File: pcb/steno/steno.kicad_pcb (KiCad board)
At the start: 2 copper layers, 200 x 50 mm, 59 parts, among them J1 Conn_01x02, K1 KEYSW, K10 KEYSW, K11 KEYSW, K12 KEYSW, K13 KEYSW, K14 KEYSW, K15 KEYSW, K16 KEYSW, K17 KEYSW, K18 KEYSW, K19 KEYSW, K2 KEYSW, K20 KEYSW, K21 KEYSW, K22 KEYSW, K23 KEYSW, K24 KEYSW, K25 KEYSW, K26 KEYSW, K27 KEYSW, K28 KEYSW, K3 KEYSW, K4 KEYSW, K5 KEYSW, K6 KEYSW, K7 KEYSW, K8 KEYSW, K9 KEYSW, U1 Adafruit_Feather

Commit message: Remove v1 files
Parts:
- removed the K2 at (70.0, 84.3)
- removed REF**: D_DO-34_SOD68_P7.62mm_Horizontal, Diode_THT:D_DO-34_SOD68_P7.62mm_Horizontal
- added D29: DIODE, Diode_THT:D_DO-34_SOD68_P7.62mm_Horizontal, B.Cu at (184.5, 95.2)
- added D30: DIODE, Diode_THT:D_DO-34_SOD68_P7.62mm_Horizontal, B.Cu at (180.7, 96.5)
- added J2: Conn_01x04, steno:OLED, F.Cu at (176.7, 112.6)
- added K1: KEYSW, Keebio-Parts:Kailh-PG1350-1u-No-Clickhole, F.Cu at (48.9, 56.9)
- added K29: KEYSW, Keebio-Parts:Kailh-PG1350-1u-No-Clickhole, F.Cu at (197.9, 78.6)
- added K30: KEYSW, Keebio-Parts:Kailh-PG1350-1u-No-Clickhole, F.Cu at (180.8, 84.3)
- added U2: MT25QL128ABA1ESE, Package_SO:SOP-8_5.28x5.23mm_P1.27mm, F.Cu at (158.2, 125.1)
- D1, D10, D11, D12, D13, D14, D15, D16, D17, D18, D19, D2, D20, D21, D22, D23, D24, D25, D26, D27, D28, D3, D4, D5, D6, D7, D8, D9: footprint Diode_SMD:D_SOD-123F -> Diode_THT:D_DO-34_SOD68_P7.62mm_Horizontal
- J1: footprint Connector_JST:JST_PH_B2B-PH-SM4-TB_1x02-1MP_P2.00mm_Vertical -> Connector_PinHeader_2.54mm:PinHeader_1x02_P2.54mm_Vertical; moved to F.Cu
- moved K25 153.5 mm to (271.9, 73.0), turned to 198.4 degrees
- moved K8 120.6 mm to (60.6, 78.7), turned to 161.6 degrees
- moved K7 119.6 mm to (43.5, 73.0), turned to 161.6 degrees
- moved K11 119.1 mm to (117.5, 78.6), turned to 161.6 degrees
- moved K23 118.5 mm to (192.5, 62.5), turned to 198.4 degrees
- moved K26 118.0 mm to (254.8, 78.7), turned to 198.4 degrees
- moved K9 117.4 mm to (83.4, 67.3), turned to 161.6 degrees
- moved K10 116.9 mm to (102.3, 67.3), turned to 161.6 degrees
- moved D11 107.8 mm to (132.9, 95.9), turned to 251.6 degrees
- moved K19 96.6 mm to (266.5, 56.8), turned to 198.4 degrees
- moved D23 94.0 mm to (182.6, 95.9), turned to 288.4 degrees
- moved D10 94.0 mm to (129.1, 94.6), turned to 251.6 degrees
- moved K16 89.3 mm to (214.5, 109.5), turned to 198.4 degrees
- moved K27 86.8 mm to (232.1, 67.3), turned to 198.4 degrees
- moved K24 85.4 mm to (175.5, 68.2), turned to 198.4 degrees
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- renumbered K1 to K2
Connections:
- D10 pad 2: COL10 -> COL4
- D11 pad 2: COL11 -> COL5
- D12 pad 2: COL1 -> COL6
- D13 pad 2: COL2 -> COL1
- D14 pad 2: COL3 -> COL2
- D15 pad 2: COL4 -> COL3
- D16 pad 2: COL5 -> COL4
- D17 pad 2: COL6 -> COL5
- D18 pad 2: COL7 -> COL6
- D19 pad 2: COL8 -> COL1
- D20 pad 2: COL9 -> COL2
- D21 pad 2: COL10 -> COL3
- D22 pad 2: COL11 -> COL4
- D23 pad 2: COL3 -> COL5
- D24 pad 2: COL4 -> COL6
- D25 pad 2: COL5 -> COL1
- D26 pad 2: COL6 -> COL2
- D27 pad 2: COL7 -> COL3
- D28 pad 2: COL8 -> COL4
- D7 pad 2: COL7 -> COL1
- D8 pad 2: COL8 -> COL2
- D9 pad 2: COL9 -> COL3
- J1 pad 1: GND -> BAT
- J1 pad 2: BAT -> GND
- K10 pad 1: ROW1 -> ROW2
- K11 pad 1: ROW1 -> ROW2
- K13 pad 1: ROW2 -> ROW3
- K14 pad 1: ROW2 -> ROW3
- K15 pad 1: ROW2 -> ROW3
- K16 pad 1: ROW2 -> ROW3
- K17 pad 1: ROW2 -> ROW3
- K18 pad 1: ROW2 -> ROW3
- K19 pad 1: ROW2 -> ROW4
- K2 pad 2: Net-(D1-Pad1) -> Net-(D2-Pad1)
- K20 pad 1: ROW2 -> ROW4
- K21 pad 1: ROW2 -> ROW4
- K22 pad 1: ROW2 -> ROW4
- K23 pad 1: ROW3 -> ROW4
- K24 pad 1: ROW3 -> ROW4
- K25 pad 1: ROW3 -> ROW5
- K26 pad 1: ROW3 -> ROW5
- K27 pad 1: ROW3 -> ROW5
- K28 pad 1: ROW3 -> ROW5
- K7 pad 1: ROW1 -> ROW2
- K8 pad 1: ROW1 -> ROW2
- K9 pad 1: ROW1 -> ROW2
- U1 pad 1: Net-(U1-Pad1) -> (no net)
- U1 pad 10: ROW3 -> COL3
- U1 pad 11: ROW2 -> COL2
- U1 pad 12: ROW1 -> COL1
- U1 pad 14: Net-(U1-Pad14) -> (no net)
- U1 pad 15: Net-(U1-Pad15) -> VCC
- U1 pad 16: RST -> (no net)
- U1 pad 18: GND -> (no net)
- U1 pad 19: Net-(U1-Pad19) -> (no net)
- U1 pad 2: COL5 -> DQ3
- U1 pad 20: Net-(U1-Pad20) -> ROW1
- U1 pad 21: Net-(U1-Pad21) -> ROW2
- U1 pad 22: COL11 -> ROW4
- U1 pad 23: COL10 -> ROW5
- U1 pad 24: Net-(U1-Pad24) -> (no net)
- U1 pad 25: COL9 -> ROW3
- U1 pad 26: COL8 -> CS
- U1 pad 27: COL7 -> SCL
- U1 pad 28: COL6 -> SDA
- U1 pad 3: COL4 -> DQ2
- U1 pad 4: Net-(U1-Pad4) -> MISO_DQ1
- U1 pad 5: Net-(U1-Pad5) -> MOSI_DQ0
- U1 pad 6: Net-(U1-Pad6) -> SCLK
- U1 pad 7: COL3 -> COL6
- U1 pad 8: COL2 -> COL5
- U1 pad 9: COL1 -> COL4
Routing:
- net ROW4: track 0.00 -> 156.3 mm, vias 0 -> 1
- net ROW5: track 0.00 -> 144.9 mm, vias 0 -> 1
- net COL11: track 88.5 -> 0.00 mm, vias 1 -> 0
- net VCC: track 0.00 -> 76.4 mm
- net Net-(D25-Pad1): track 10.9 -> 84.8 mm
- net Net-(D19-Pad1): track 17.5 -> 89.2 mm
- net COL10: track 69.5 -> 0.00 mm, vias 1 -> 0
- net COL5: track 10.1 -> 65.9 mm
- net Net-(D20-Pad1): track 17.2 -> 70.3 mm
- net COL9: track 50.5 -> 0.00 mm, vias 1 -> 0
- net Net-(D26-Pad1): track 14.5 -> 64.2 mm
- net Net-(D1-Pad1): track 33.0 -> 82.4 mm
- net Net-(D21-Pad1): track 17.5 -> 63.7 mm
- net COL4: track 27.8 -> 72.6 mm, vias 1 -> 0
- net COL6: track 10.8 -> 55.6 mm
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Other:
- board size 200 x 50 mm -> 250.8 x 91.5 mm
- board text added: "BAT"
- board text added: "GND"

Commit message: Update PCB
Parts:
- D1, D10, D11, D12, D13, D14, D15, D16, D17, D18, D19, D2, D20, D21, D22, D23, D24, D25, D26, D27, D28, D29, D3, D30, D4, D5, D6, D7, D8, D9: footprint Diode_THT:D_DO-34_SOD68_P7.62mm_Horizontal -> Diode_SMD:D_SOD-123; moved to F.Cu
- U1: value Adafruit_Feather -> nice_nano; footprint Downloads:ADAFRUIT_FEATHER -> nice-nano-kicad:nice_nano
- moved D19 74.5 mm to (249.0, 32.1), turned to 216.8 degrees
- moved D7 71.1 mm to (46.5, 116.5), turned to 180 degrees
- moved D25 70.6 mm to (259.2, 45.7), turned to 216.8 degrees
- moved D1 68.2 mm to (46.5, 99.5), turned to 180 degrees
- moved D8 60.6 mm to (64.5, 116.5), turned to 180 degrees
- moved D20 60.5 mm to (234.6, 42.9), turned to 216.8 degrees
- moved D2 57.5 mm to (64.5, 99.5), turned to 180 degrees
- moved D26 56.3 mm to (244.8, 56.5), turned to 216.8 degrees
- moved D21 55.1 mm to (209.4, 39.2), turned to 216.8 degrees
- moved D22 48.9 mm to (191.4, 45.2), turned to 216.8 degrees
- moved D27 45.3 mm to (219.6, 52.8), turned to 216.8 degrees
- moved D3 44.4 mm to (82.5, 81.5), turned to 180 degrees
- moved D15 44.4 mm to (148.5, 133.0), turned to 180 degrees
- moved D14 44.0 mm to (130.5, 133.0), turned to 180 degrees
- moved D13 42.9 mm to (112.5, 133.0), turned to 180 degrees
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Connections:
- U1 pad 1: (no net) -> ROW1
- U1 pad 10: COL3 -> COL6
- U1 pad 11: COL2 -> Net-(U1-Pad11)
- U1 pad 12: COL1 -> CS
- U1 pad 13: GND -> ROW3
- U1 pad 14: (no net) -> MOSI_DQ0
- U1 pad 15: VCC -> MISO_DQ1
- U1 pad 16: (no net) -> SCLK
- U1 pad 17: BAT -> COL2
- U1 pad 18: (no net) -> COL1
- U1 pad 19: (no net) -> ROW4
- U1 pad 2: DQ3 -> ROW2
- U1 pad 20: ROW1 -> ROW5
- U1 pad 21: ROW2 -> VCC
- U1 pad 22: ROW4 -> RST
- U1 pad 23: ROW5 -> GND
- U1 pad 24: (no net) -> BAT
- U1 pad 3: DQ2 -> GND
- U1 pad 4: MISO_DQ1 -> GND
- U1 pad 5: MOSI_DQ0 -> SCL
- U1 pad 6: SCLK -> SDA
- U1 pad 7: COL6 -> COL3
- U1 pad 8: COL5 -> COL4
- U1 pad 9: COL4 -> COL5
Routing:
- net COL1: track 102.0 -> 297.2 mm, vias 0 -> 2
- net COL2: track 90.2 -> 263.9 mm, vias 0 -> 2
- net COL3: track 80.5 -> 248.4 mm, vias 0 -> 2
- net COL4: track 72.6 -> 214.5 mm, vias 0 -> 2
- net COL5: track 65.9 -> 173.4 mm, vias 0 -> 2
- net COL6: track 55.6 -> 144.5 mm, vias 0 -> 2
- net Net-(D19-Pad1): track 89.2 -> 9.69 mm
- net Net-(D25-Pad1): track 84.8 -> 9.69 mm
- net Net-(D1-Pad1): track 82.4 -> 9.69 mm
- net Net-(D7-Pad1): track 71.3 -> 9.69 mm
- net Net-(D20-Pad1): track 70.3 -> 9.69 mm
- net Net-(D3-Pad1): track 65.3 -> 9.69 mm
- net Net-(D26-Pad1): track 64.2 -> 9.69 mm
- net Net-(D21-Pad1): track 63.7 -> 9.69 mm
- net Net-(D2-Pad1): track 62.9 -> 9.69 mm
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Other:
- board size 250.8 x 91.5 mm -> 231.4 x 120.7 mm

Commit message: First PCB version
- Use raw MCU
- Use 5x6 matrix and 30keys (like steno phone)
- Use SOD-123 diodes (like steno phone)
- Use 2.2in TFT for better UX(?)
- Lots of ground plane!
- Add (fake?) logo and contributors
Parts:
- removed J2: Conn_01x04, steno:OLED
- added C1: 22pF, Capacitor_SMD:C_0603_1608Metric, F.Cu at (133.5, 110.0)
- added C10: 1uF, Capacitor_SMD:C_0805_2012Metric, F.Cu at (159.0, 115.5)
- added C11: 1uF, Capacitor_SMD:C_0805_2012Metric, F.Cu at (158.0, 120.5)
- added C2: 22pF, Capacitor_SMD:C_0603_1608Metric, F.Cu at (133.5, 100.0)
- added C3: 1uF, Capacitor_SMD:C_0805_2012Metric, F.Cu at (156.0, 102.0)
- added C4: 1uF, Capacitor_SMD:C_0805_2012Metric, F.Cu at (146.5, 96.0)
- added C5: 0.1uF, Capacitor_SMD:C_0603_1608Metric, F.Cu at (138.5, 103.0)
- added C6: 0.1uF, Capacitor_SMD:C_0603_1608Metric, F.Cu at (155.0, 98.0)
- added C7: 0.1uF, Capacitor_SMD:C_0603_1608Metric, F.Cu at (143.0, 114.0)
- added C8: 10uF, Capacitor_SMD:C_0805_2012Metric, F.Cu at (156.0, 109.0)
- added C9: 1uF, Capacitor_SMD:C_0805_2012Metric, F.Cu at (160.0, 108.0)
- added F1: Polyfuse_Small, Fuse:Fuse_1206_3216Metric_Castellated, F.Cu at (151.0, 76.5)
- added G***: LOGO, misc:batwings, F.Cu at (196.0, 98.5)
- added R1: 10k, Resistor_SMD:R_0805_2012Metric, F.Cu at (144.0, 78.0)
- added R2: 22, Resistor_SMD:R_0603_1608Metric, F.Cu at (148.2, 84.9)
- added R3: 22, Resistor_SMD:R_0603_1608Metric, F.Cu at (149.7, 84.9)
- added R4: 10k, Resistor_SMD:R_0805_2012Metric, F.Cu at (156.0, 112.0)
- added R5: 10k, Resistor_SMD:R_0805_2012Metric, F.Cu at (153.4, 128.0)
- added SW1: SW_Push, Button_Switch_SMD:SW_SPST_B3U-1000P, F.Cu at (140.5, 69.7)
- added U3: MCP1700-3302E_SOT23, Package_TO_SOT_SMD:SOT-23, F.Cu at (160.0, 111.0)
- added U4: LCD2.2in, steno:LCD2.2in, F.Cu at (148.5, 105.1)
- added Y1: 16MHz, Crystal:Crystal_SMD_EuroQuartz_MJ-4Pin_5.0x3.2mm_HandSoldering, F.Cu at (133.5, 105.0)
- J1: value Conn_01x02 -> USB_mini_micro_B; footprint Connector_PinHeader_2.54mm:PinHeader_1x02_P2.54mm_Vertical -> Connector_USB:AMPHENOL_10118192-0001LF
- K1, K10, K11, K12, K13, K14, K15, K16, K17, K18, K19, K2, K20, K21, K22, K23, K24, K25, K26, K27, K28, K29, K3, K30, K4, K5, K6, K7, K8, K9: value KEYSW -> SW_Push
- U1: value nice_nano -> ATmega32U4-AU; footprint nice-nano-kicad:nice_nano -> Package_QFP:TQFP-44_10x10mm_P0.8mm
- moved D7 43.2 mm to (21.6, 81.1), turned to 161.6 degrees
- moved K7 42.2 mm to (23.0, 76.9), turned to 161.6 degrees
- moved D1 39.6 mm to (26.9, 65.0), turned to 161.6 degrees
- moved K19 39.3 mm to (268.8, 60.7), turned to 198.4 degrees
- moved D8 39.3 mm to (38.7, 86.8), turned to 161.6 degrees
- moved D19 39.1 mm to (270.2, 65.0), turned to 198.4 degrees
- moved D25 39.0 mm to (275.6, 81.1), turned to 198.4 degrees
- moved K25 39.0 mm to (274.1, 76.9), turned to 198.4 degrees
- moved K1 38.7 mm to (28.4, 60.7), turned to 161.6 degrees
- moved K8 38.2 mm to (40.1, 82.5), turned to 161.6 degrees
- moved D13 35.3 mm to (80.4, 118.1), turned to 161.6 degrees
- moved D2 35.3 mm to (44.0, 70.7), turned to 161.6 degrees
- moved K2 34.3 mm to (45.4, 66.4), turned to 161.6 degrees
- moved D14 34.2 mm to (97.5, 123.8), turned to 161.6 degrees
- moved D15 34.1 mm to (114.6, 129.5), turned to 161.6 degrees
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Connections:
- net RST renamed Net-(U1-Pad22)
- J1 pad 1: BAT -> VCC
- J1 pad 2: GND -> D-
- U1 pad 1: ROW1 -> Net-(U1-Pad1)
- U1 pad 10: COL6 -> MOSI
- U1 pad 11: Net-(U1-Pad11) -> MISO
- U1 pad 12: CS -> Net-(U1-Pad12)
- U1 pad 13: ROW3 -> Net-(R1-Pad1)
- U1 pad 14: MOSI_DQ0 -> +5V
- U1 pad 15: MISO_DQ1 -> GND
- U1 pad 16: SCLK -> Net-(C2-Pad1)
- U1 pad 17: COL2 -> Net-(C1-Pad1)
- U1 pad 18: COL1 -> LITE
- U1 pad 19: ROW4 -> ROW1
- U1 pad 2: ROW2 -> +5V
- U1 pad 20: ROW5 -> ROW2
- U1 pad 21: VCC -> ROW3
- U1 pad 24: BAT -> +5V
- U1 pad 3: GND -> Net-(R3-Pad1)
- U1 pad 30: GND -> COL6
- U1 pad 31: Net-(U1-Pad31) -> CS
- U1 pad 32: DQ3 -> Net-(U1-Pad32)
- U1 pad 33: DQ2 -> Net-(R4-Pad2)
- U1 pad 34: BAT -> +5V
- U1 pad 4: GND -> Net-(R2-Pad1)
- U1 pad 5: SCL -> GND
- U1 pad 6: SDA -> Net-(C4-Pad1)
- U1 pad 7: COL3 -> +5V
- U1 pad 8: COL4 -> Net-(U1-Pad8)
- U1 pad 9: COL5 -> SCLK
- U2 pad 2: MISO_DQ1 -> MISO
- U2 pad 3: DQ2 -> Net-(R5-Pad1)
- U2 pad 4: GND -> GND1
- U2 pad 5: MOSI_DQ0 -> MOSI
- U2 pad 7: DQ3 -> Net-(R5-Pad1)
- U2 pad 8: VCC -> +3V3
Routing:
- net +5V: track 0.00 -> 98.9 mm, vias 0 -> 8
- net VCC: track 50.2 -> 4.31 mm
- net MISO: track 0.00 -> 45.8 mm, vias 0 -> 3
- net LCD_CS: track 0.00 -> 45.0 mm, vias 0 -> 1
- net MOSI: track 0.00 -> 44.8 mm, vias 0 -> 2
- net C\D: track 0.00 -> 44.4 mm, vias 0 -> 1
- net LCD_RST: track 0.00 -> 44.0 mm, vias 0 -> 1
- net Net-(R1-Pad1): track 0.00 -> 38.6 mm
- net SDA: track 37.5 -> 0.00 mm
- net SCL: track 37.1 -> 0.00 mm
- net GND: track 74.0 -> 108.0 mm, vias 0 -> 11
- net COL1: track 297.2 -> 330.5 mm, vias 2 -> 3
- net LITE: track 0.00 -> 32.5 mm
- net SCLK: track 20.4 -> 52.2 mm, vias 1 -> 3
- net +3V3: track 0.00 -> 31.5 mm
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- added copper zone on B.Cu, net GND
- added copper zone on F.Cu, net GND
- added copper zone on B.Cu, net GND1
- added copper zone on F.Cu, net GND1
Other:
- board size 231.4 x 120.7 mm -> 270.1 x 95.3 mm
- net class Default: clearance 0.2 -> 0.2032; trace_width 0.25 -> 0.254
- rule trace_clearance: 0.2 -> 0.2032
- rule trace_min: 0.2 -> 0.254
- board text added: "BatWings Embedded steno gives you wings!"
- board text added: "Part of a senior project @ UIUC ECE 445 By: - Haoqing "Steven" Zhu - Rishi Krishnan - Soham Karanjikar Open sourced @ github.com/crides/steno"
- board text removed: "BAT"
- board text removed: "GND"

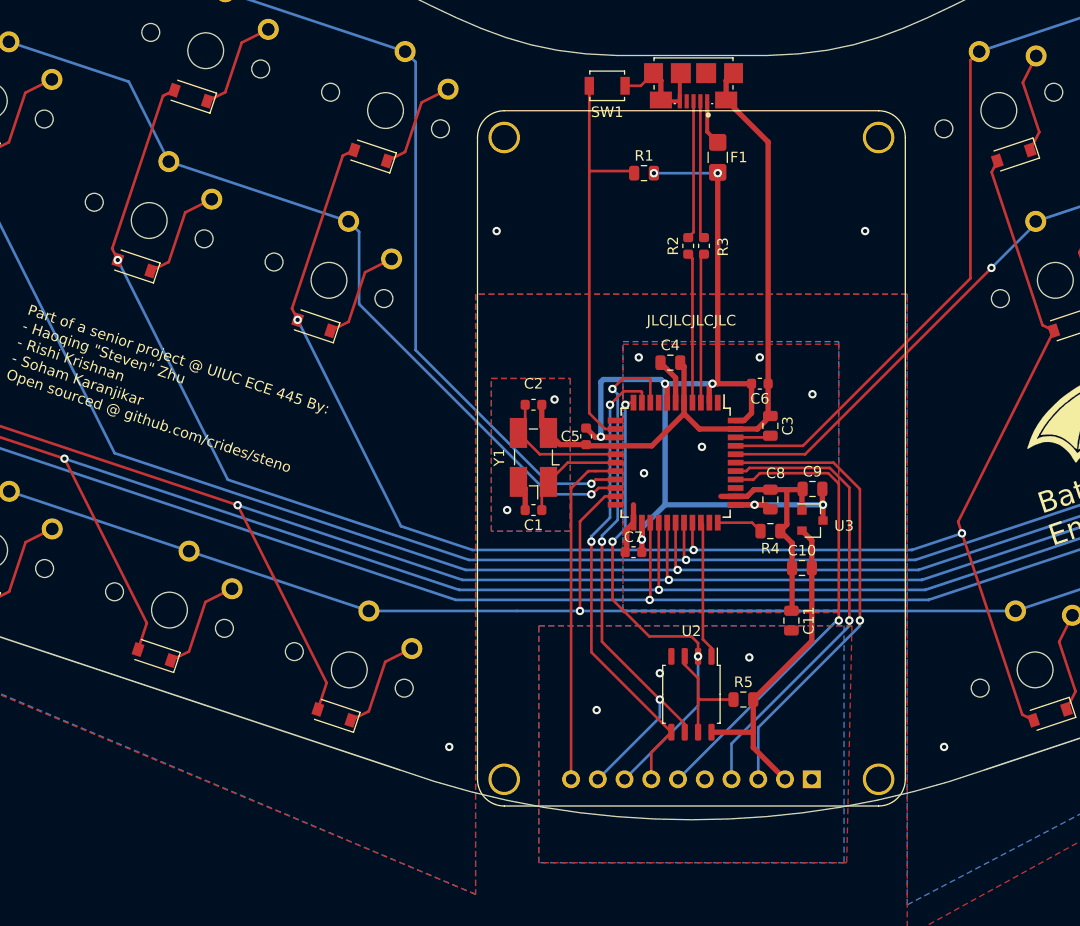
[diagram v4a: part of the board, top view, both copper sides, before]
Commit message: [PCB] Final changes
- Add bumper locations on silkscreen
- Add hex buffer for level shifting
- Unify the 2 grounds into 1, removing the decoupling cap
- Add MCU peripheral ref & value to silkscreen
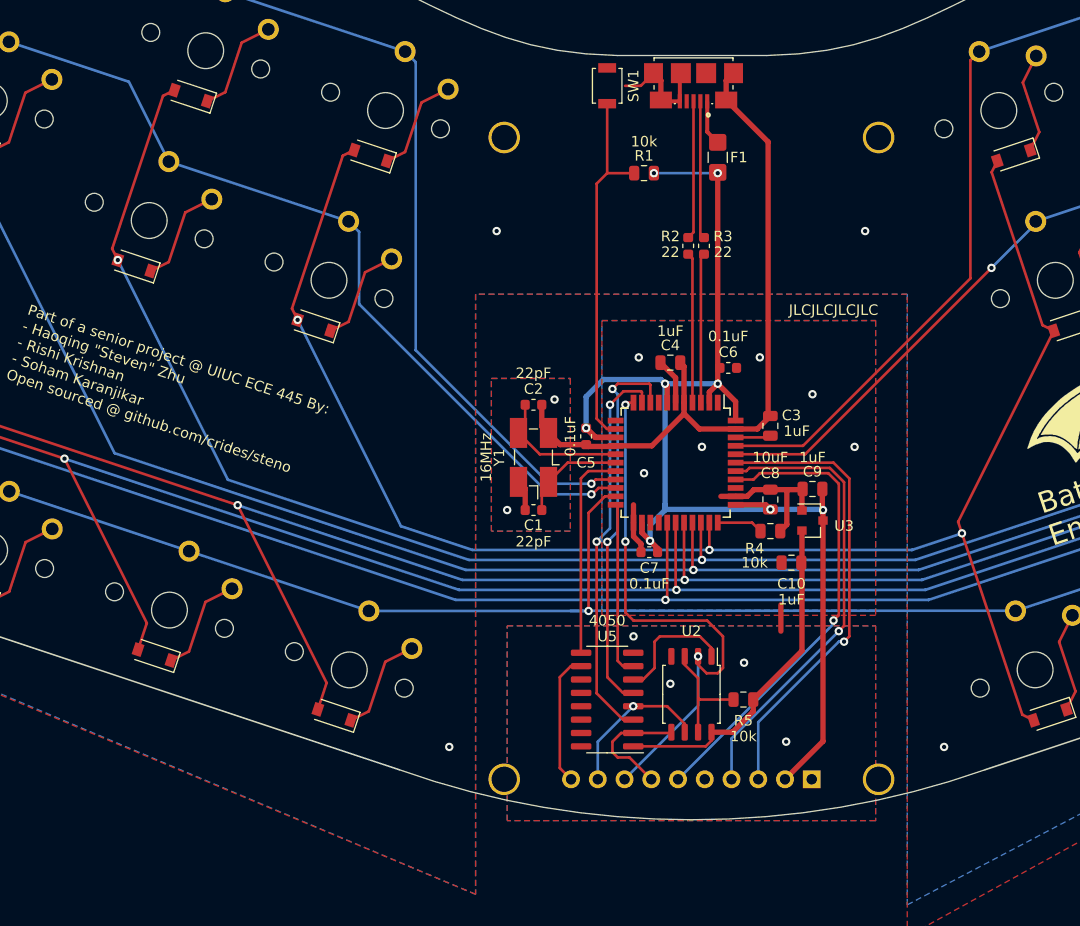
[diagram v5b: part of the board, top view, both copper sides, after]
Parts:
- removed C11: 1uF, Capacitor_SMD:C_0805_2012Metric
- added U5: 4050, Package_SO:SOIC-16_3.9x9.9mm_P1.27mm, F.Cu at (140.5, 128.0)
- R2, R3: value 22 -> 22
- moved C6 3.35 mm to (152.0, 96.5)
- moved C7 1.50 mm to (144.5, 114.0)
- moved C10 1.12 mm to (158.0, 115.0)
- turned SW1 to 270 degrees
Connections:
- U1 pad 10: MOSI -> MOSI_5V
- U1 pad 18: LITE -> LITE_5V
- U1 pad 22: Net-(U1-Pad22) -> CS_5V
- U1 pad 25: COL1 -> Net-(U1-Pad25)
- U1 pad 26: COL2 -> Net-(U1-Pad26)
- U1 pad 27: COL3 -> COL1
- U1 pad 28: COL4 -> COL2
- U1 pad 29: COL5 -> COL3
- U1 pad 30: COL6 -> COL4
- U1 pad 31: CS -> COL5
- U1 pad 32: Net-(U1-Pad32) -> COL6
- U1 pad 9: SCLK -> SCLK_5V
- U2 pad 1: CS -> CS_3V3
- U2 pad 4: GND1 -> GND
- U2 pad 5: MOSI -> MOSI_3V3
- U2 pad 6: SCLK -> SCLK_3V3
- U4 pad 1: GND1 -> GND
- U4 pad 10: LITE -> LITE_3V3
- U4 pad 2: +3V3 -> +5V
- U4 pad 7: MOSI -> MOSI_3V3
- U4 pad 9: SCLK -> SCLK_3V3
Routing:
- net SCLK: track 52.2 -> 0.00 mm, vias 3 -> 0
- net MOSI: track 44.8 -> 0.00 mm, vias 2 -> 0
- net MOSI_5V: track 0.00 -> 37.0 mm, vias 0 -> 2
- net SCLK_5V: track 0.00 -> 36.6 mm, vias 0 -> 2
- net LITE: track 32.5 -> 0.00 mm
- net +5V: track 98.9 -> 124.0 mm
- net LITE_5V: track 0.00 -> 20.2 mm
- net CS_5V: track 0.00 -> 16.6 mm
- net SCLK_3V3: track 0.00 -> 14.7 mm, vias 0 -> 1
- net CS: track 13.1 -> 0.00 mm
- net LITE_3V3: track 0.00 -> 12.6 mm
- net CS_3V3: track 0.00 -> 12.3 mm
- net MOSI_3V3: track 0.00 -> 11.7 mm
- net MISO: track 45.8 -> 52.3 mm
- net GND: track 108.0 -> 102.6 mm, vias 11 -> 16
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- removed copper zone on B.Cu, net GND1
- removed copper zone on F.Cu, net GND1
